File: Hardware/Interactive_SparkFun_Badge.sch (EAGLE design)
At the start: 27 parts, among them J1 AVR_SPI_PRG_6PTH, U1 ATMEGA328P

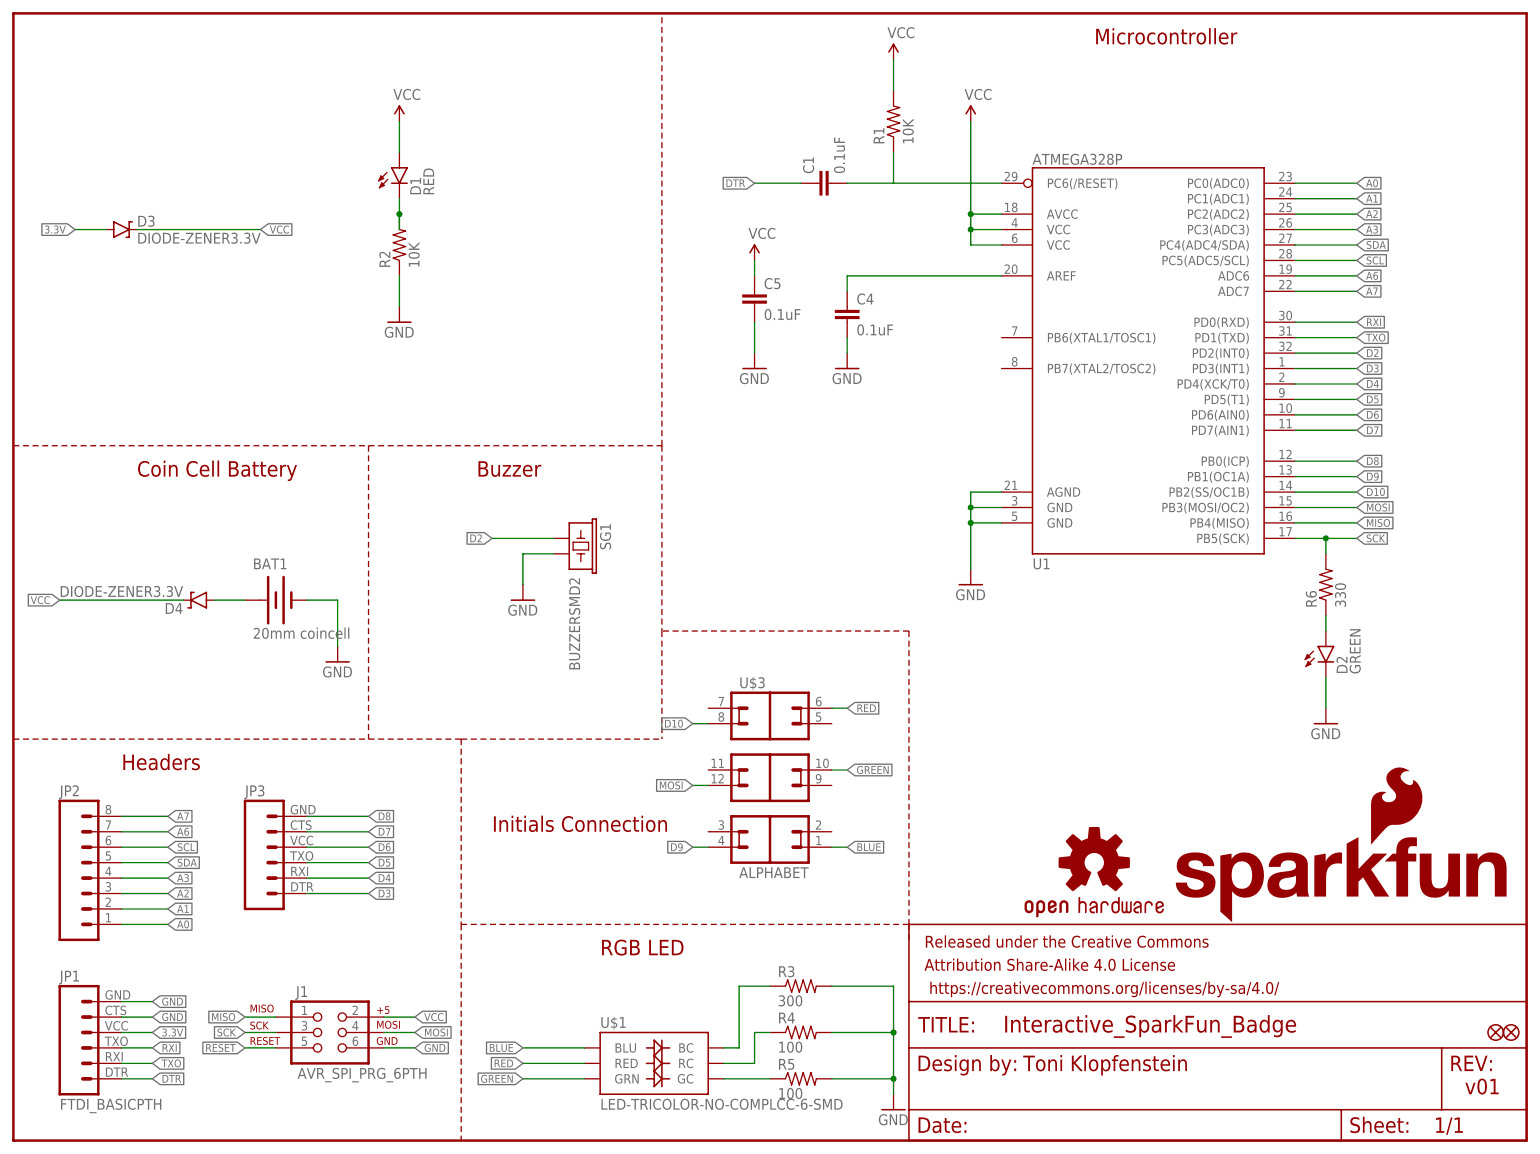
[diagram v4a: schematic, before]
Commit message: Updating to new power circuit, and adding front silk
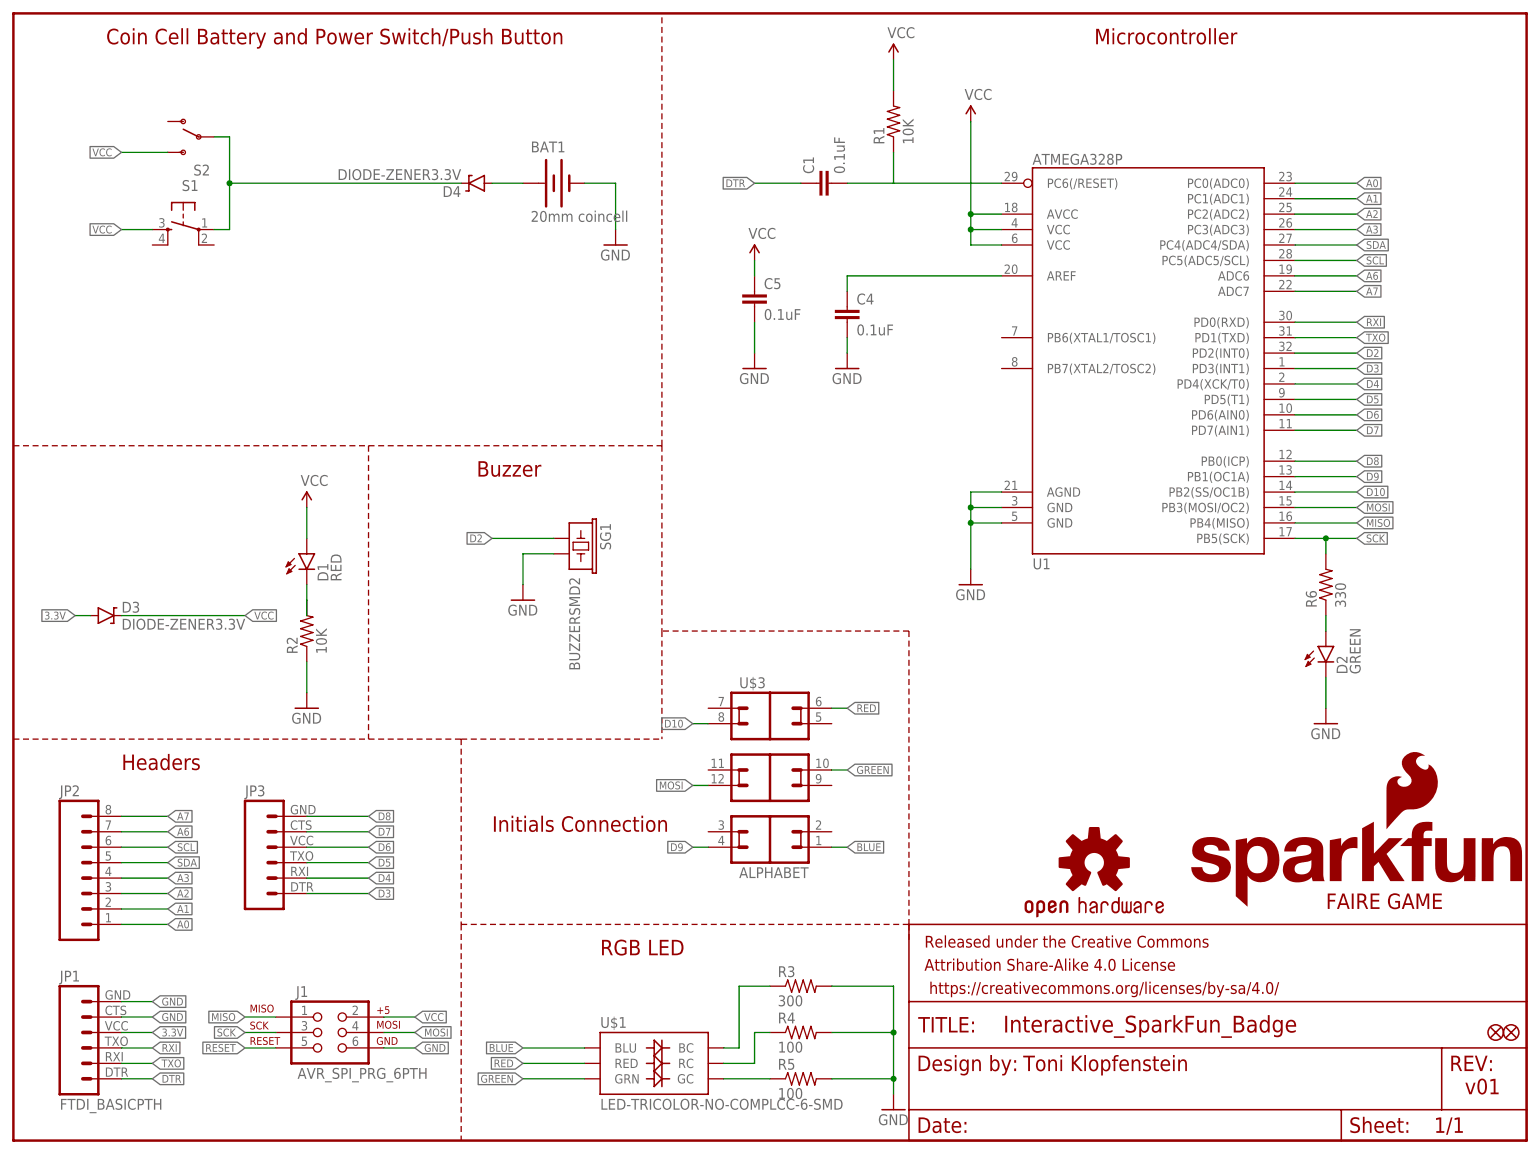
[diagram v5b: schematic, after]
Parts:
- removed LOGO2: SFE_LOGO_NAME_FLAME.3_INCH, SparkFun-Aesthetics:SFE_LOGO_NAME_FLAME.3_INCH
- added S1: (no value), SparkFun-Electromechanical:TAC_SWITCHSMD
- added S2: (no value), SparkFun-Electromechanical:SWITCH-SPDTSMD
- added U$4: FAIRE_GAME_SILK, Local Library:FAIRE_GAME_SILK
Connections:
- new net N$1: D4.C, S1.1, S2.P
- net VCC: now also S1.3, S2.S; no longer D4.C
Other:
- note added: "Coin Cell Battery and Power Switch/Push Button"
- note removed: "Coin Cell Battery"
- moved on the sheet: BAT1, D1, D3, D4, R2

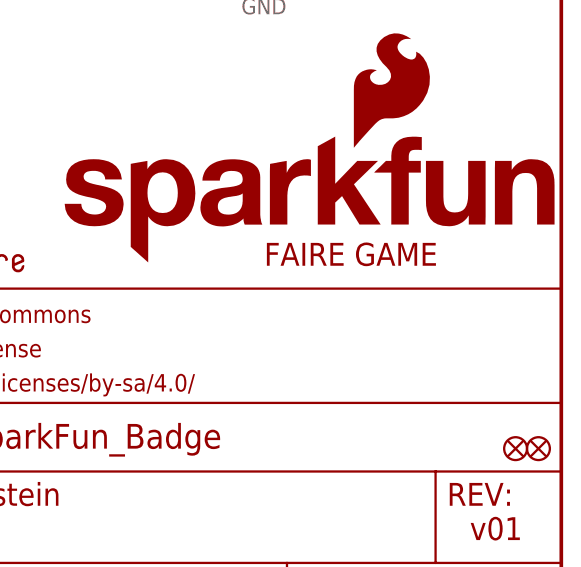
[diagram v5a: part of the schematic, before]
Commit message: Adding NY MF silk
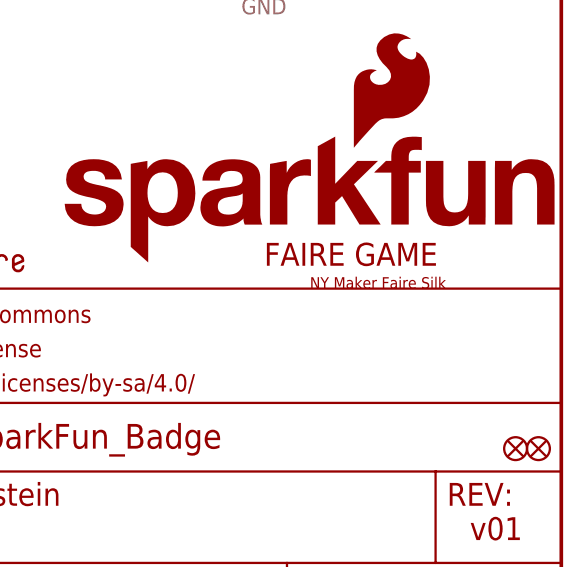
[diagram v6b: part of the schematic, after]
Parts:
- added U$2: NY_FAIRE_BACK, Local Library:NY_FAIRE_BACK
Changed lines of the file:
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@@
 <?xml version="1.0" encoding="utf-8"?>
 <!DOCTYPE eagle SYSTEM "eagle.dtd">
-<eagle version="6.5.0">
+<eagle version="6.6.0">
 <drawing>
 <settings>
@@
 <part name="S2" library="SparkFun-Electromechanical" deviceset="SWITCH-SPDT" device="SMD"/>
 <part name="U$4" library="Local Library" deviceset="FAIRE_GAME_SILK" device=""/>
+<part name="U$2" library="Local Library" deviceset="NY_FAIRE_BACK" device=""/>
 </parts>
 <sheets>
@@
 <instance part="S2" gate="1" x="30.48" y="165.1" rot="MR0"/>
 <instance part="U$4" gate="G$1" x="193.04" y="38.1"/>
+<instance part="U$2" gate="G$1" x="220.98" y="35.56"/>
 </instances>
 <busses>
